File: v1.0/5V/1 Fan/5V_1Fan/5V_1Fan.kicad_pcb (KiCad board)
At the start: 2 copper layers, 50 x 40 mm, 21 parts, among them J1 Conn_01x03_Pin, J2 Conn_01x02, J3 Conn_01x04, J4 Conn_01x02, J5 Conn_01x03, Q1 2N7002, Q2 Q_PMOS_GSD, U1 ATtiny402-SS

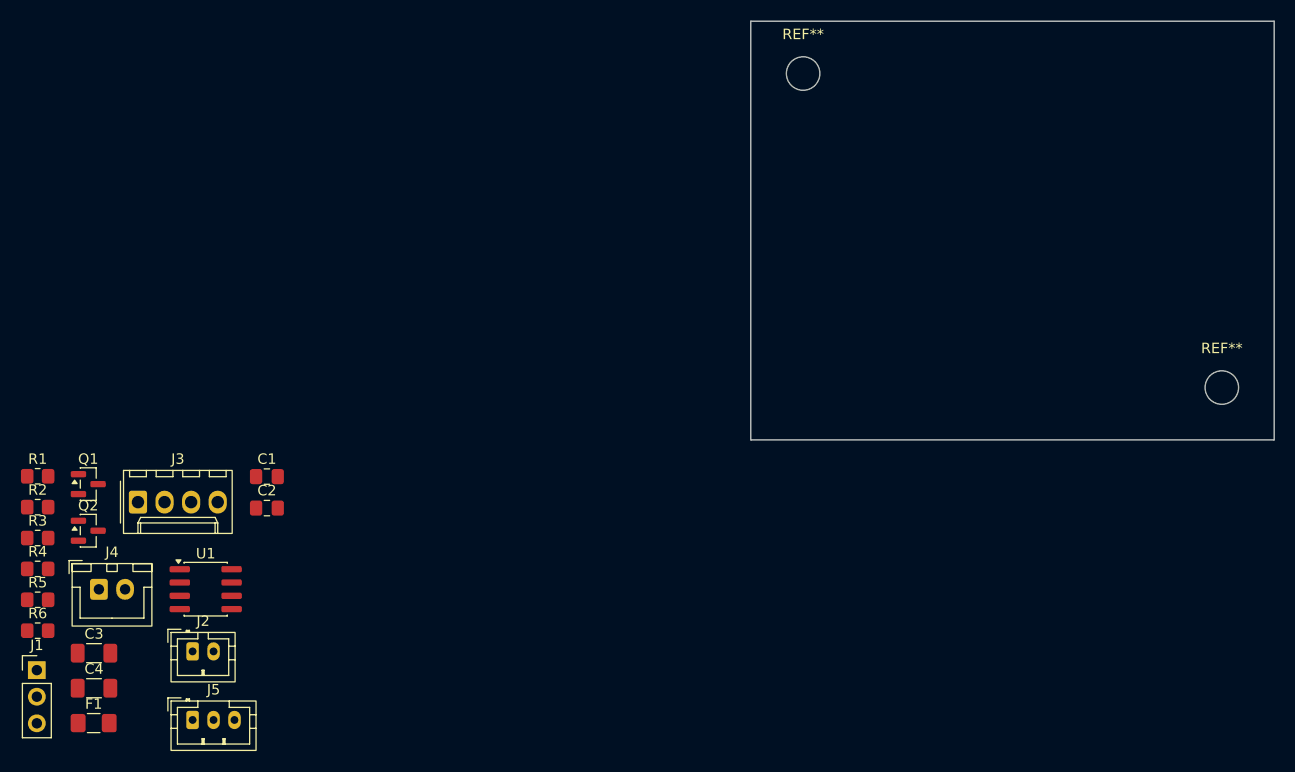
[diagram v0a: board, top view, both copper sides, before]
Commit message: 5v 1fan 1th
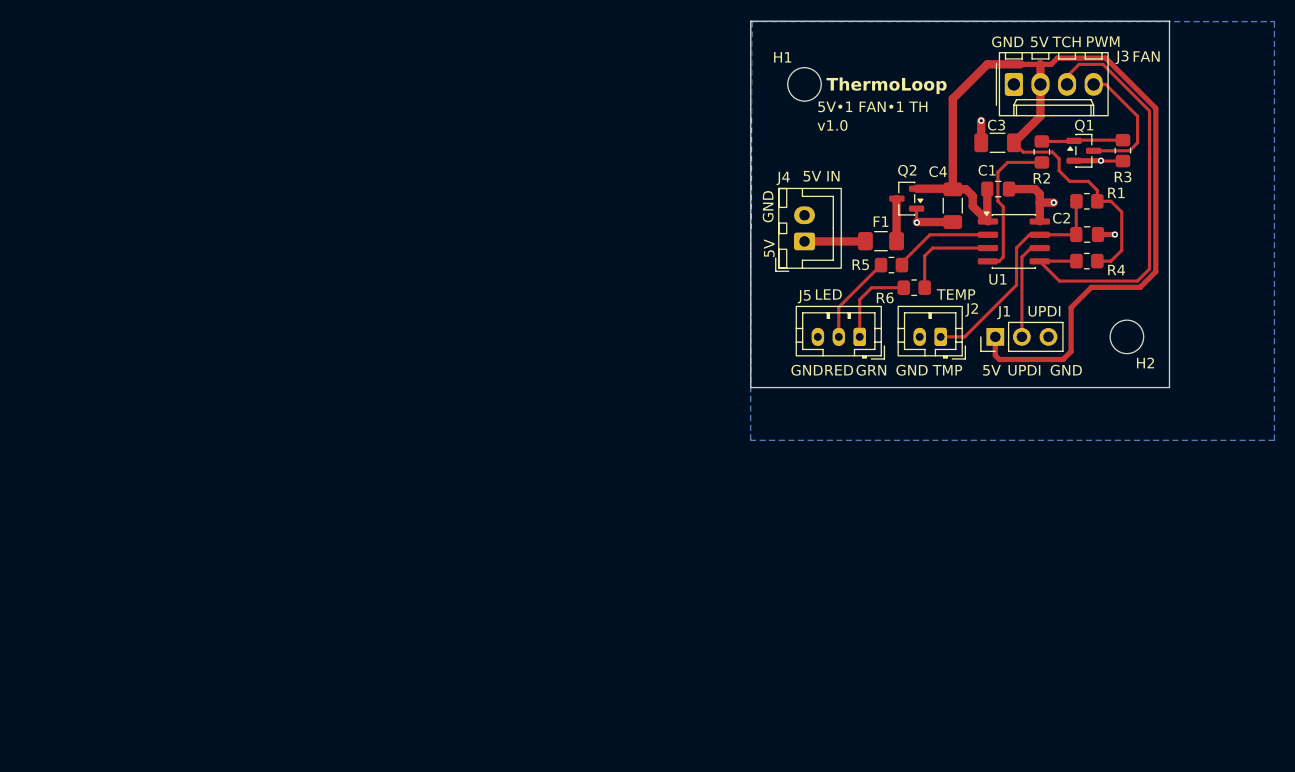
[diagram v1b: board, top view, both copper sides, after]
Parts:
- moved R3 110.1 mm to (185.6, 62.4), turned to 90 degrees
- moved R4 104.5 mm to (182.1, 72.9), turned to 180 degrees
- moved R1 103.6 mm to (182.1, 67.2)
- moved R2 101.8 mm to (177.8, 62.5), turned to -90 degrees
- moved Q1 100.3 mm to (181.8, 62.4)
- moved C3 99.1 mm to (173.6, 61.6)
- moved J1 96.9 mm to (173.4, 80.2), turned to 90 degrees
- moved C4 94.1 mm to (169.3, 67.6), turned to -90 degrees
- moved J3 92.7 mm to (175.1, 56.0)
- moved R6 89.9 mm to (165.6, 75.5)
- moved F1 88.2 mm to (162.4, 71.0)
- moved R5 87.6 mm to (163.4, 73.3)
- moved Q2 84.4 mm to (164.9, 67.0), turned to 180 degrees
- moved U1 84.1 mm to (175.1, 71.0)
- moved C2 82.6 mm to (182.1, 70.4)
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- renumbered REF** to H1, REF** to H2
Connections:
- U1 pad 2: /GREEN_LED -> /RED_LED
- U1 pad 3: /RED_LED -> /GREEN_LED
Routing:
- net +5V: track 0.00 -> 111.5 mm
- net /FAN_TACH: track 0.00 -> 41.3 mm
- net /TEMP_SENSE: track 0.00 -> 22.3 mm
- net GND: track 0.00 -> 20.3 mm, vias 0 -> 5
- net Net-(U1-PA1): track 0.00 -> 14.5 mm
- net /FAN_PWM: track 0.00 -> 12.5 mm
- net Net-(J1-Pin_2): track 0.00 -> 9.69 mm
- net /RED_LED: track 0.00 -> 9.55 mm
- net /GREEN_LED: track 0.00 -> 9.39 mm
- net Net-(J5-Pin_2): track 0.00 -> 8.53 mm
- net Net-(J5-Pin_1): track 0.00 -> 8.24 mm
- net Net-(Q1-G): track 0.00 -> 7.80 mm
- net +5V_INPUT: track 0.00 -> 5.83 mm
- net Net-(Q2-D): track 0.00 -> 4.08 mm
- added copper zone on B.Cu, net GND
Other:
- board size 50 x 40 mm -> 40 x 35 mm
- board text added: "2026-08"
- board text added: "5V"
- board text added: "5V IN"
- board text added: "5V•1 FAN•1 TH"
- board text added: "FAN"
- board text added: "GND"
- board text added: "GRN"
- board text added: "LED"
- board text added: "PWM"
- board text added: "RED"
- board text added: "TCH"
- board text added: "TEMP"
- board text added: "TMP"
- board text added: "ThermoLoop"
- board text added: "UPDI"
- board text added: "v1.0"

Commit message: updated files
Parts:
- F1: value 250mA -> 250mA PPTC
- J3: footprint Connector_Molex:Molex_KK-254_AE-6410-04A_1x04_P2.54mm_Vertical -> Connector:FanPinHeader_1x04_P2.54mm_Vertical
- Q2: value Q_PMOS_GSD -> AO3401A
- U1: value ATtiny402-SS -> ATTINY402-SSF
- moved J3 0.60 mm to (175.1, 56.6)
- moved J4 0.57 mm to (155.7, 71.0)
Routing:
- net +5V: track 111.5 -> 112.3 mm
- net /FAN_TACH: track 41.3 -> 40.8 mm
